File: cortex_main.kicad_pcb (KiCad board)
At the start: 2 copper layers, 119.4 x 119.4 mm, 30 parts, among them P1 CONN_01X05, P10 CONN_01X03, P11 CONN_01X03, P12 CONN_01X03, P13 CONN_01X03, P14 CONN_01X03, P15 CONN_01X03, P16 CONN_01X02, P17 CONN_01X02, P18 CONN_01X02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

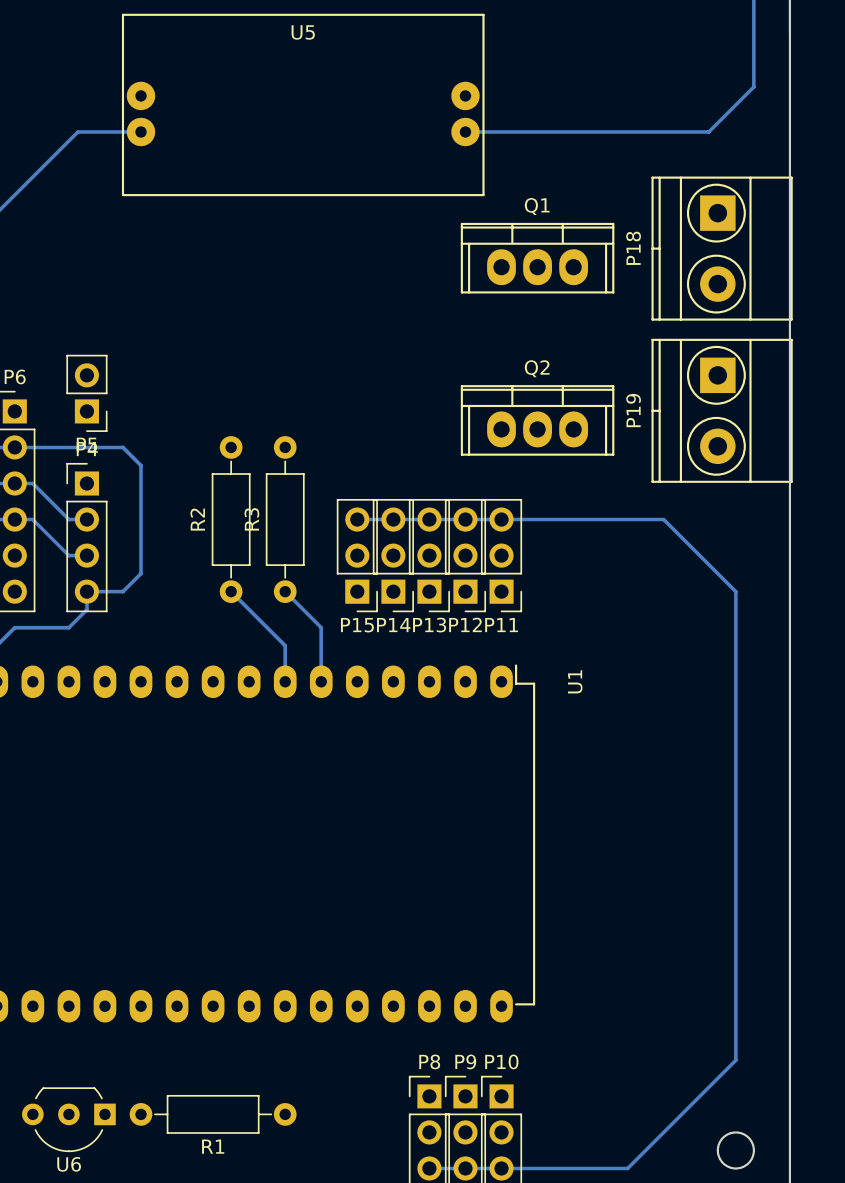
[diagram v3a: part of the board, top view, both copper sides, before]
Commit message: cortex: add clamping diode to arm motor mosfet
Signed-off-by: Yannick Gicquel <ygicquel@gmail.com>
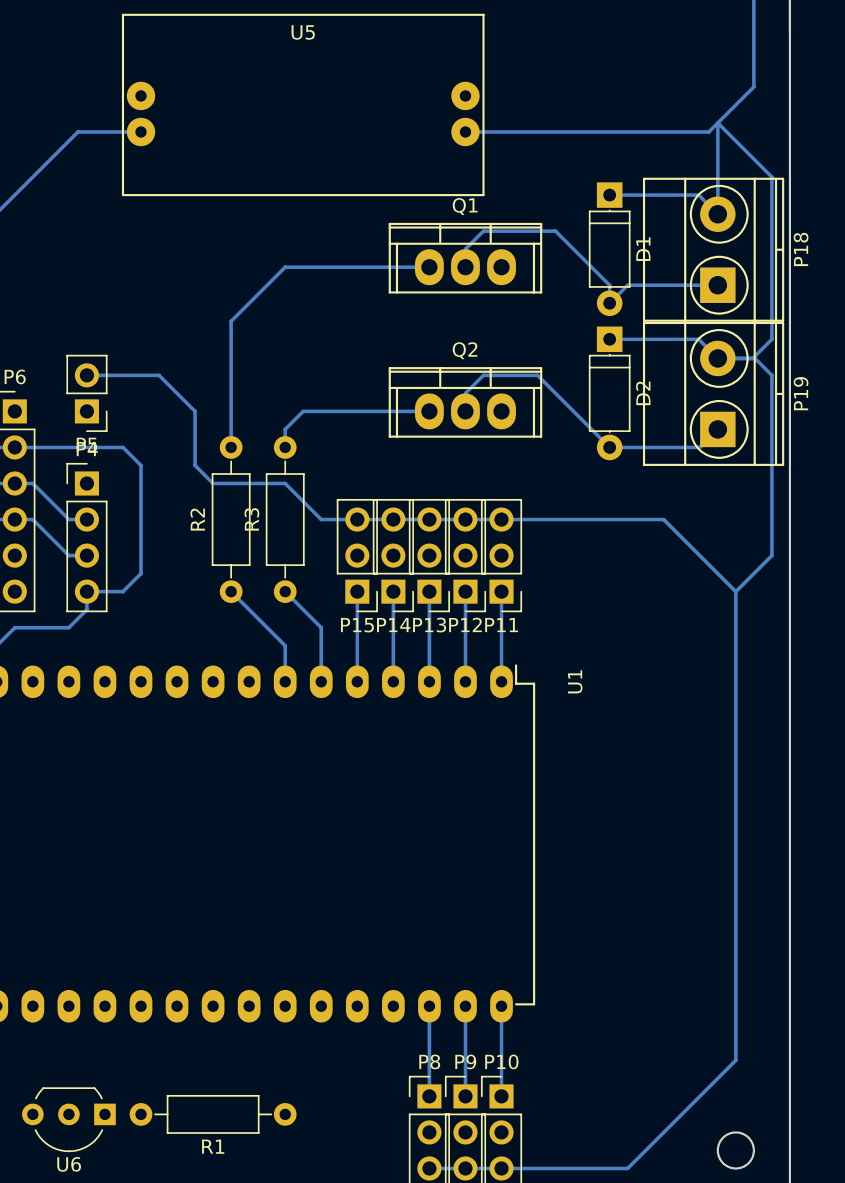
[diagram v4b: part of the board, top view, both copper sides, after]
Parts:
- added D1: 1N4001, Diodes_ThroughHole:D_A-405_P7.62mm_Horizontal, F.Cu at (142.2, 97.8)
- added D2: 1N4001, Diodes_ThroughHole:D_A-405_P7.62mm_Horizontal, F.Cu at (142.2, 108.0)
- moved Q2 5.24 mm to (132.1, 113.0)
- moved P18 5.08 mm to (149.9, 104.1), turned to 90 degrees
- moved Q1 5.08 mm to (132.1, 102.9)
- moved P19 3.81 mm to (149.9, 114.3), turned to 90 degrees
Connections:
- net +5V renamed OUTP_ARMMOTOR_L
- net OUT_ARMMOTOR_L renamed OUTN_ARMMOTOR_L
- net OUT_ARMMOTOR_R renamed OUTN_ARMMOTOR_R
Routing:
- net OUTP_ARMMOTOR_L: track 138.2 -> 228.3 mm
- net Net-(Q1-Pad1): track 0.00 -> 24.4 mm
- net OUTN_ARMMOTOR_L: track 0.00 -> 23.0 mm
- net OUTN_ARMMOTOR_R: track 0.00 -> 22.2 mm
- net Net-(Q2-Pad1): track 0.00 -> 12.0 mm
- net IR_VIN_7: track 0.00 -> 6.35 mm
- net IR_VIN_6: track 0.00 -> 6.35 mm
- net IR_VIN_5: track 0.00 -> 6.35 mm
- net IR_VIN_4: track 0.00 -> 6.35 mm
- net IR_VIN_3: track 0.00 -> 6.35 mm
- net IR_VIN_2: track 0.00 -> 6.35 mm
- net IR_VIN_1: track 0.00 -> 6.35 mm
- net IR_VIN_0: track 0.00 -> 6.35 mm

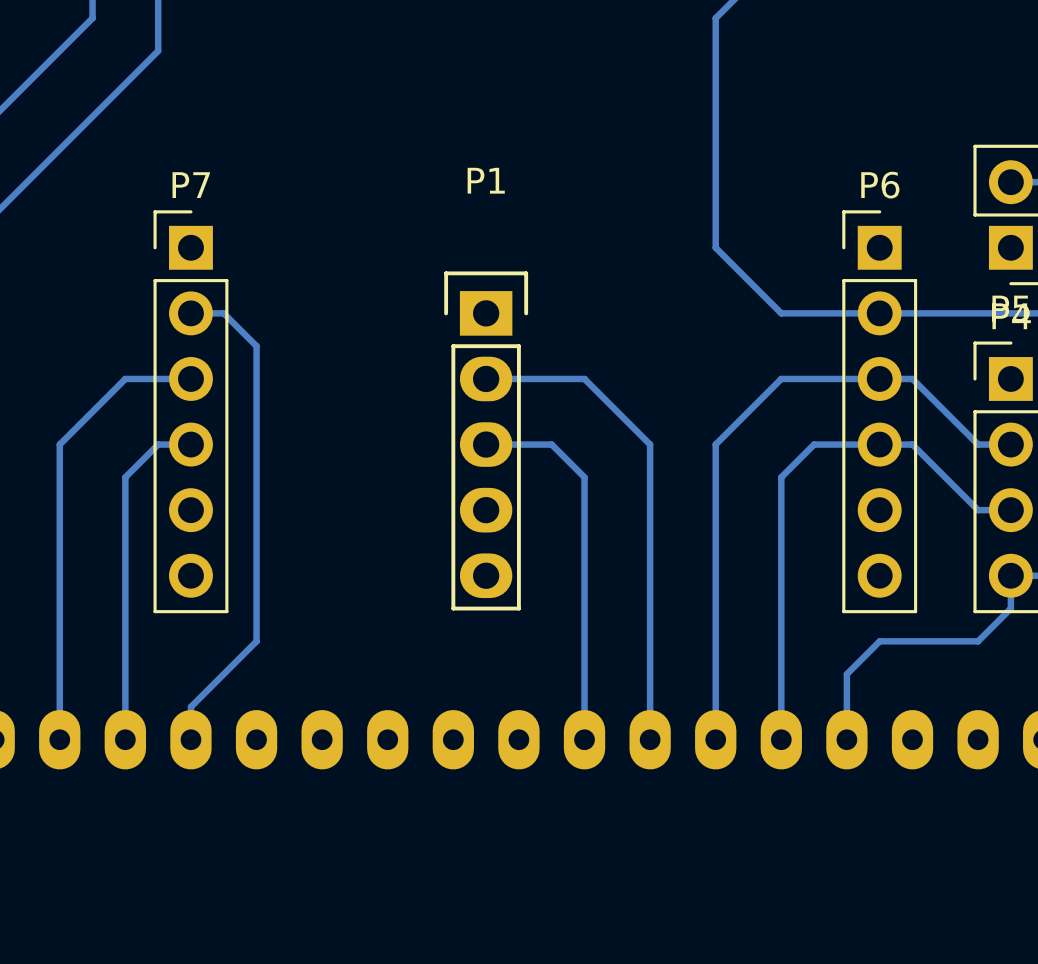
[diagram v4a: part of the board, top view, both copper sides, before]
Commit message: cortex: update UART connector
move to 4pins and wire the +3V3 supply for comm module.

Signed-off-by: Yannick Gicquel <ygicquel@gmail.com>
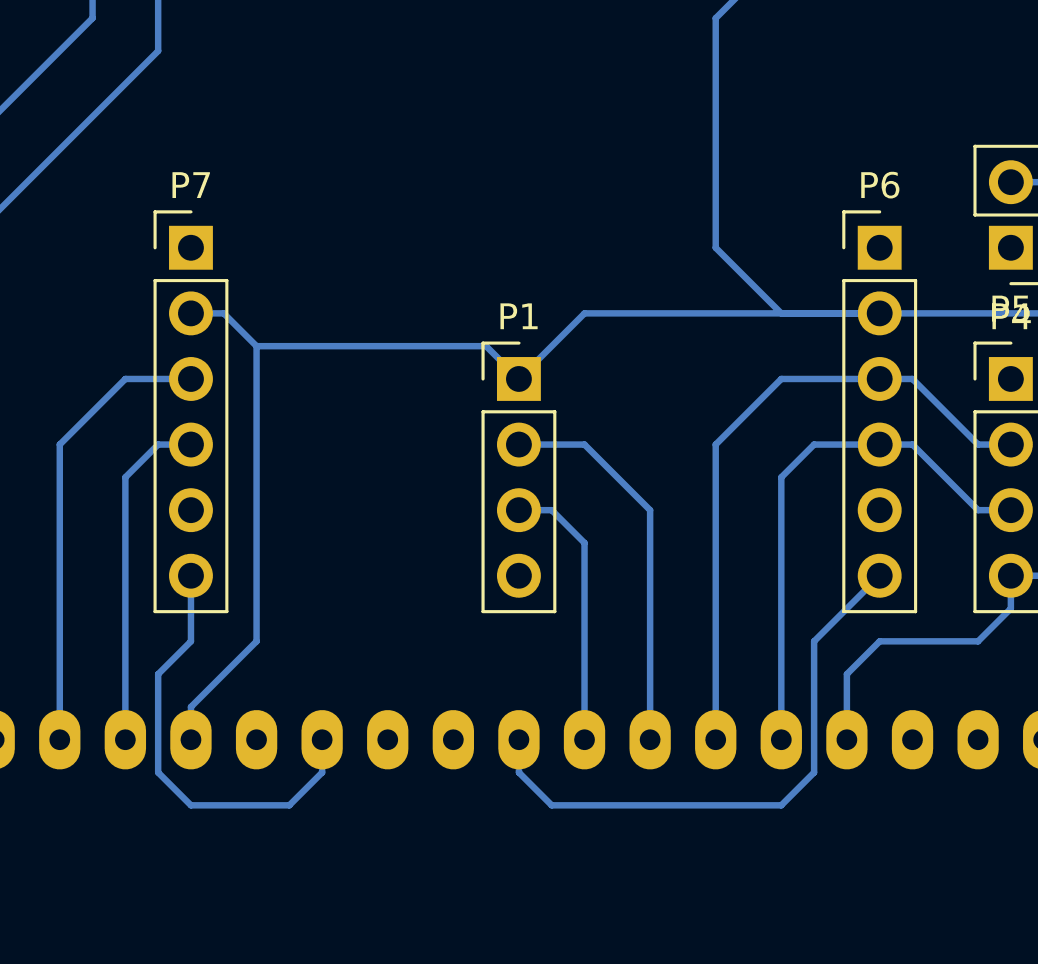
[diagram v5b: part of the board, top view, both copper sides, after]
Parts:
- P1: value CONN_01X05 -> CONN_01X04; footprint Pin_Headers:Pin_Header_Straight_1x05 -> Pin_Headers:Pin_Header_Straight_1x04_Pitch2.54mm
- moved P1 2.84 mm to (86.4, 118.1)
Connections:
- P1 pad 1: Net-(P1-Pad1) -> +3V3
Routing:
- net +3V3: track 87.9 -> 113.7 mm
- net /Sheet_Connectors/RGB_LEDEN_L: track 0.00 -> 22.4 mm
- net /Sheet_Connectors/RGB_LEDEN_R: track 0.00 -> 16.8 mm
- net /Sheet_Connectors/UART_DBG_TXD: track 18.8 -> 15.0 mm
- net /Sheet_Connectors/UART_DBG_RXD: track 14.5 -> 10.7 mm

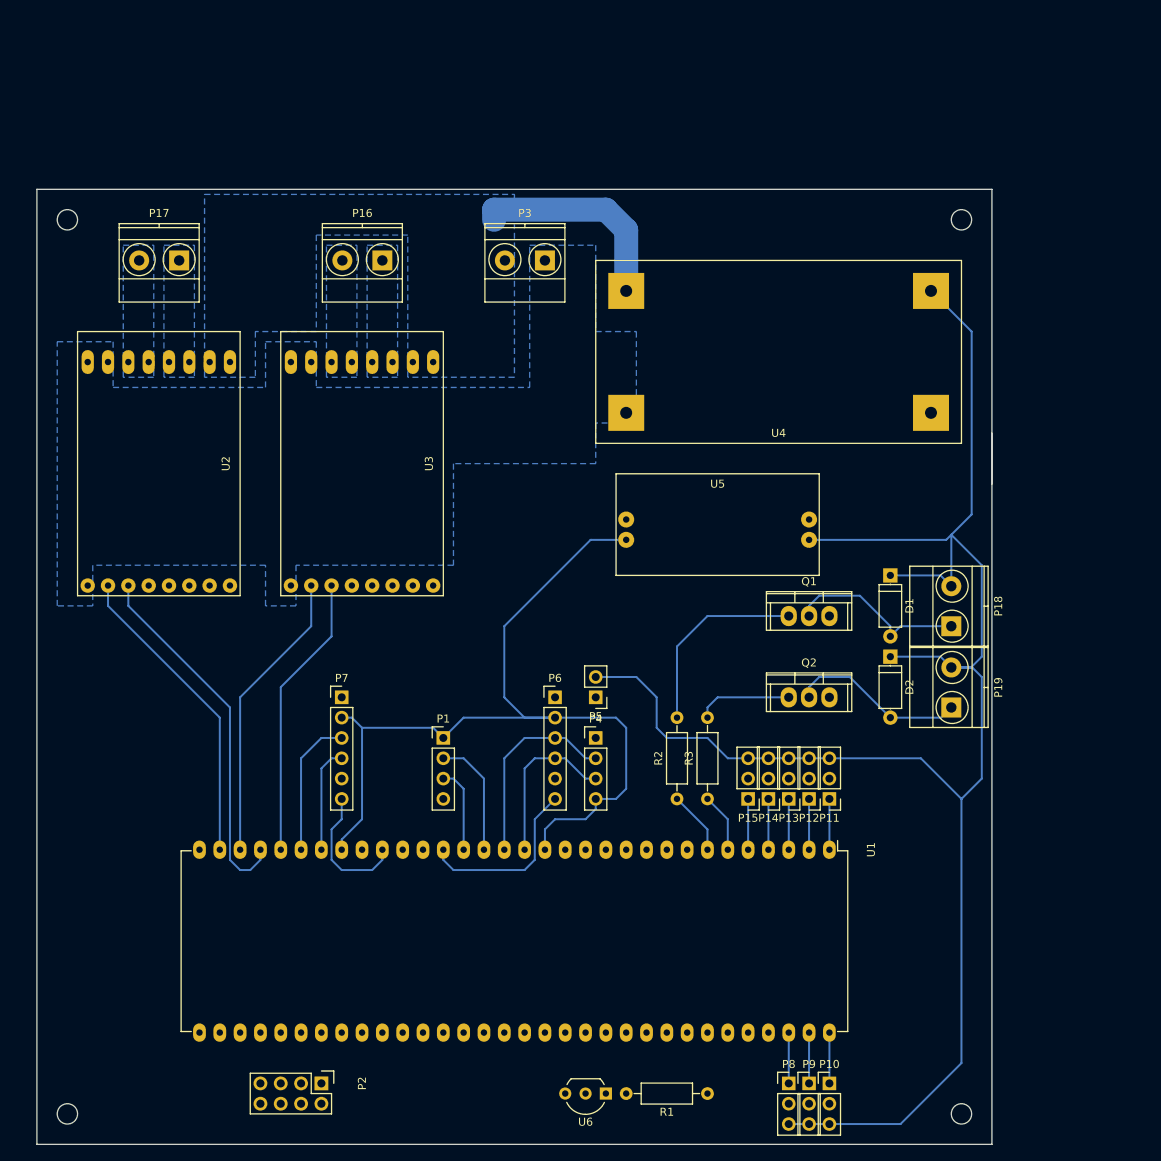
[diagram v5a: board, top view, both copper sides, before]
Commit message: cortex: sch & pcb updates after first review
- add testpad on pololu /rst signals
- fix rotary encoders pinout: [+,-,A,B]
- add jumper to choose 3V3 or 5V for IR sharp sensors

Signed-off-by: Yannick Gicquel <ygicquel@gmail.com>
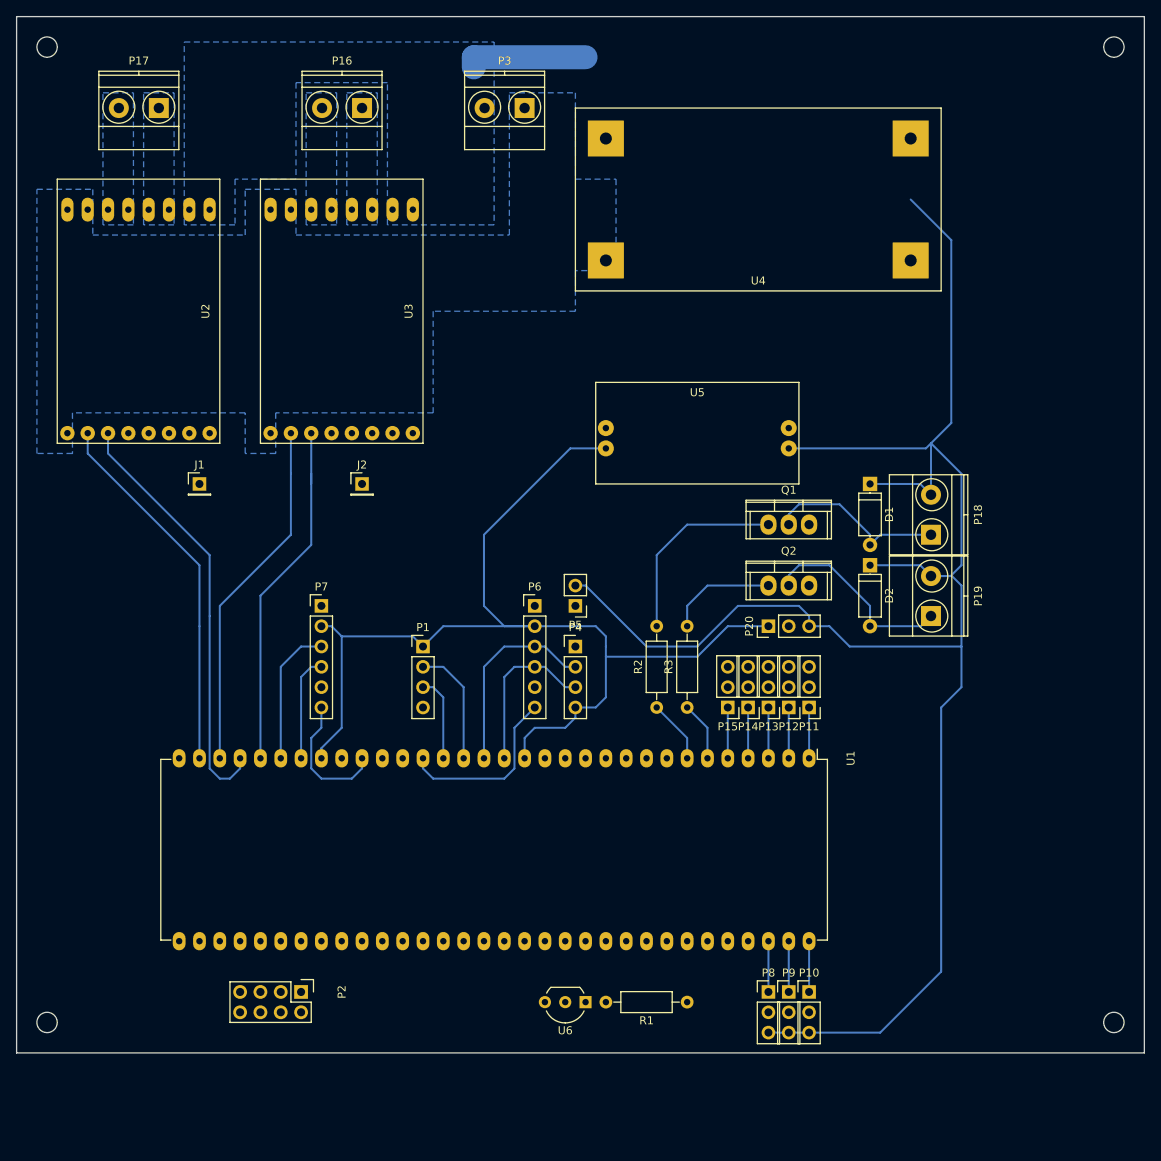
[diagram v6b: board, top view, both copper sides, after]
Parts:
- added J1: TEST_1P, Pin_Headers:Pin_Header_Straight_1x01_Pitch2.54mm, F.Cu at (55.9, 86.4)
- added J2: TEST_1P, Pin_Headers:Pin_Header_Straight_1x01_Pitch2.54mm, F.Cu at (76.2, 86.4)
- added P20: CONN_01X03, Pin_Headers:Pin_Header_Straight_1x03_Pitch2.54mm, F.Cu at (127.0, 104.1)
- moved P17 19.2 mm to (50.8, 39.4)
- moved P3 19.2 mm to (96.5, 39.4)
- moved P16 19.2 mm to (76.2, 39.4)
- moved U3 19.2 mm to (73.7, 64.8)
- moved U4 19.2 mm to (125.7, 50.8)
- moved U2 19.2 mm to (48.3, 64.8)
- moved Q2 14.2 mm to (129.5, 99.1)
- moved D1 11.7 mm to (139.7, 86.4)
- moved D2 11.7 mm to (139.7, 96.5)
- moved P12 11.7 mm to (129.5, 114.3)
- moved P18 11.7 mm to (147.3, 92.7)
- moved Q1 11.7 mm to (129.5, 91.4)
- moved P14 11.7 mm to (124.5, 114.3)
- moved U6 11.7 mm to (104.1, 151.1)
- moved P11 11.7 mm to (132.1, 114.3)
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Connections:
- P10 pad 3: OUTP_ARMMOTOR_L -> IR_VCC
- P11 pad 3: OUTP_ARMMOTOR_L -> IR_VCC
- P12 pad 3: OUTP_ARMMOTOR_L -> IR_VCC
- P13 pad 3: OUTP_ARMMOTOR_L -> IR_VCC
- P14 pad 3: OUTP_ARMMOTOR_L -> IR_VCC
- P15 pad 3: OUTP_ARMMOTOR_L -> IR_VCC
- P2 pad 5: +3V3 -> GND
- P2 pad 6: +3V3 -> GND
- P2 pad 7: GND -> +3V3
- P2 pad 8: GND -> +3V3
- P8 pad 3: OUTP_ARMMOTOR_L -> IR_VCC
- P9 pad 3: OUTP_ARMMOTOR_L -> IR_VCC
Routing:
- net +24V: track 26.5 -> 0.00 mm
- net +3V3: track 113.7 -> 135.6 mm
- net (no net): track 0.00 -> 15.2 mm
- net IR_VCC: track 0.00 -> 14.0 mm
- net OUTP_ARMMOTOR_L: track 228.3 -> 216.4 mm
- net /Sheet_MCU/PWM_R: track 35.7 -> 44.5 mm
- net /Sheet_MCU/PWM_L: track 45.7 -> 53.3 mm
- net /Sheet_MCU/DIR_L: track 38.8 -> 46.4 mm
- net /Sheet_MCU/DIR_R: track 36.7 -> 44.3 mm
- net OUTN_ARMMOTOR_R: track 22.2 -> 24.7 mm
- net Net-(Q2-Pad1): track 12.0 -> 13.8 mm
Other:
- board size 119.4 x 119.4 mm -> 141 x 129.5 mm
